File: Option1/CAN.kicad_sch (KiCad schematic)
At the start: 6 parts, among them U1 TJA1051T-3

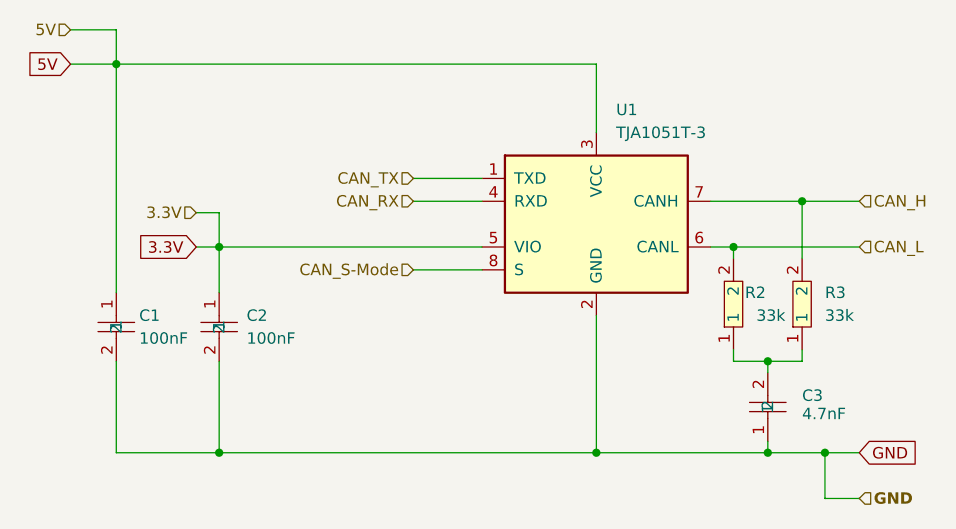
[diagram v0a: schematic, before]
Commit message: SPI Flash hinzugefügt, IN/Outputs vereinheitlicht, USB Flash Möglichkeit hinzugefügt, Display fehtl noch
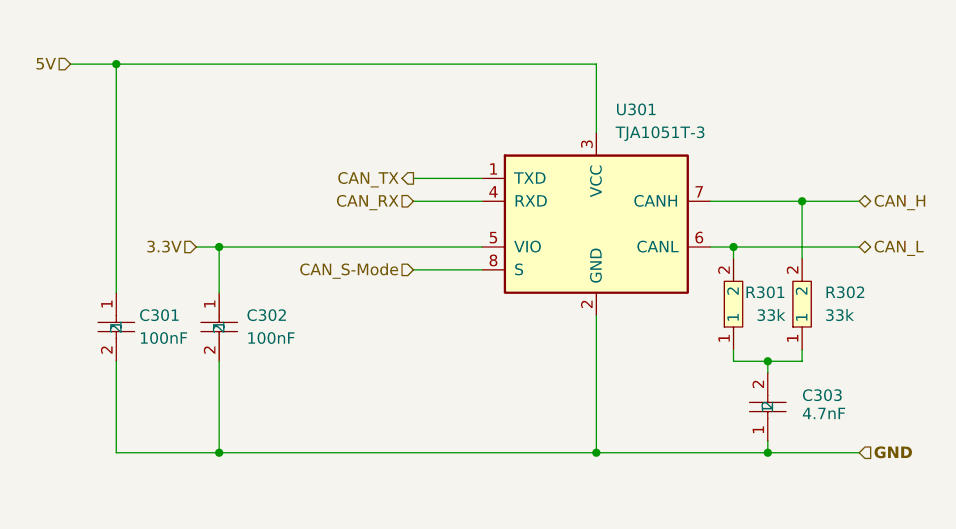
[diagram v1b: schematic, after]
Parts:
- renumbered C1 to C301, C2 to C302, C3 to C303, R2 to R301, R3 to R302, U1 to U301
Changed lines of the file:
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@@
 (kicad_sch
-	(version 20231120)
+	(version 20250114)
 	(generator "eeschema")
-	(generator_version "8.0")
+	(generator_version "9.0")
 	(paper "A4")
 	(title_block
@@
 	)
 	(junction
-		(at 167.64 121.92)
-		(diameter 0)
-		(color 0 0 0 0)
-	)
-	(junction
 		(at 161.29 111.76)
 		(diameter 0)
@@
 	(wire
 		(pts
-			(xy 167.64 121.92) (xy 161.29 121.92)
+			(xy 161.29 121.92) (xy 171.45 121.92)
 		)
 		(stroke
@@
 	(wire
 		(pts
-			(xy 171.45 121.92) (xy 167.64 121.92)
-		)
-		(stroke
-			(width 0)
-			(type default)
-		)
-	)
-	(wire
-		(pts
 			(xy 100.33 99.06) (xy 100.33 104.14)
 		)
@@
 	(wire
 		(pts
-			(xy 88.9 74.93) (xy 88.9 78.74)
-		)
-		(stroke
-			(width 0)
-			(type default)
-		)
-	)
-	(wire
-		(pts
 			(xy 157.48 99.06) (xy 171.45 99.06)
 		)
@@
 	(wire
 		(pts
-			(xy 97.79 95.25) (xy 100.33 95.25)
+			(xy 97.79 99.06) (xy 100.33 99.06)
 		)
 		(stroke
@@
 	(wire
 		(pts
-			(xy 167.64 127) (xy 167.64 121.92)
-		)
-		(stroke
-			(width 0)
-			(type default)
-		)
-	)
-	(wire
-		(pts
-			(xy 97.79 99.06) (xy 100.33 99.06)
-		)
-		(stroke
-			(width 0)
-			(type default)
-		)
-	)
-	(wire
-		(pts
 			(xy 165.1 111.76) (xy 161.29 111.76)
 		)
@@
 	(wire
 		(pts
-			(xy 83.82 74.93) (xy 88.9 74.93)
+			(xy 83.82 78.74) (xy 88.9 78.74)
 		)
 		(stroke
@@
 	(wire
 		(pts
-			(xy 171.45 127) (xy 167.64 127)
-		)
-		(stroke
-			(width 0)
-			(type default)
-		)
-	)
-	(wire
-		(pts
 			(xy 121.92 93.98) (xy 129.54 93.98)
 		)
@@
 	(wire
 		(pts
-			(xy 100.33 95.25) (xy 100.33 99.06)
-		)
-		(stroke
-			(width 0)
-			(type default)
-		)
-	)
-	(wire
-		(pts
 			(xy 154.94 99.06) (xy 157.48 99.06)
 		)
@@
 	(wire
 		(pts
-			(xy 88.9 78.74) (xy 83.82 78.74)
-		)
-		(stroke
-			(width 0)
-			(type default)
-		)
-	)
-	(wire
-		(pts
 			(xy 161.29 121.92) (xy 161.29 120.65)
 		)
@@
 			(width 0)
 			(type default)
-		)
-	)
-	(global_label "GND"
-		(shape input)
-		(at 171.45 121.92 0)
-		(fields_autoplaced yes)
-		(effects
-			(font
-				(size 1.27 1.27)
-			)
-			(justify left)
-		)
-		(property "Intersheetrefs" "${INTERSHEET_REFS}"
-			(at 178.3057 121.92 0)
-			(effects
-				(font
-					(size 1.27 1.27)
-				)
-				(justify left)
-				(hide yes)
-			)
-		)
-	)
-	(global_label "3.3V"
-		(shape input)
-		(at 97.79 99.06 180)
-		(fields_autoplaced yes)
-		(effects
-			(font
-				(size 1.27 1.27)
-			)
-			(justify right)
-		)
-		(property "Intersheetrefs" "${INTERSHEET_REFS}"
-			(at 90.6924 99.06 0)
-			(effects
-				(font
-					(size 1.27 1.27)
-				)
-				(justify right)
-				(hide yes)
-			)
-		)
-	)
-	(global_label "5V"
-		(shape input)
-		(at 83.82 78.74 180)
-		(fields_autoplaced yes)
-		(effects
-			(font
-				(size 1.27 1.27)
-			)
-			(justify right)
-		)
-		(property "Intersheetrefs" "${INTERSHEET_REFS}"
-			(at 78.5367 78.74 0)
-			(effects
-				(font
-					(size 1.27 1.27)
-				)
-				(justify right)
-				(hide yes)
-			)
 		)
 	)
@@
 	(hierarchical_label "GND"
 		(shape input)
-		(at 171.45 127 0)
+		(at 171.45 121.92 0)
 		(effects
 			(font
@@
 	)
 	(hierarchical_label "CAN_TX"
-		(shape input)
+		(shape output)
 		(at 121.92 91.44 180)
 		(effects
@@
 	(hierarchical_label "3.3V"
 		(shape input)
-		(at 97.79 95.25 180)
+		(at 97.79 99.06 180)
 		(effects
 			(font
@@
 	)
 	(hierarchical_label "CAN_L"
-		(shape input)
+		(shape bidirectional)
 		(at 171.45 99.06 0)
 		(effects
@@
 	(hierarchical_label "5V"
 		(shape input)
-		(at 83.82 74.93 180)
+		(at 83.82 78.74 180)
 		(effects
 			(font
@@
 	)
 	(hierarchical_label "CAN_H"
-		(shape input)
+		(shape bidirectional)
 		(at 171.45 93.98 0)
 		(effects
@@
 		(dnp no)
 		(fields_autoplaced yes)
-		(property "Reference" "U1"
-			(at 144.4341 83.82 0)
+		(property "Reference" "U301"
+			(at 144.3833 83.82 0)
 			(effects
 				(font
@@
 		)
 		(property "Value" "TJA1051T-3"
-			(at 144.4341 86.36 0)
+			(at 144.3833 86.36 0)
 			(effects
 				(font
@@
 			(project "Option1"
 				(path "/b9e5f262-9648-4b79-bdd1-af888b822329/09daa8db-a615-4efc-9912-47e942ec8e61"
-					(reference "U1")
+					(reference "U1701")
 					(unit 1)
 				)
@@
 		(on_board yes)
 		(dnp no)
-		(property "Reference" "R2"
+		(property "Reference" "R301"
 			(at 158.75 104.14 90)
 			(effects
@@
 			(project "Option1"
 				(path "/b9e5f262-9648-4b79-bdd1-af888b822329/09daa8db-a615-4efc-9912-47e942ec8e61"
-					(reference "R2")
+					(reference "R1701")
 					(unit 1)
 				)
 				(path "/b9e5f262-9648-4b79-bdd1-af888b822329/149ab29c-8f38-45ea-932f-f5c39c8a8ac3"
-					(reference "R?")
+					(reference "R301")
 					(unit 1)
 				)
@@
 		(on_board yes)
 		(dnp no)
-		(property "Reference" "C1"
+		(property "Reference" "C301"
 			(at 91.44 106.68 90)
 			(effects
@@
 			(project "Option1"
 				(path "/b9e5f262-9648-4b79-bdd1-af888b822329/09daa8db-a615-4efc-9912-47e942ec8e61"
-					(reference "C1")
+					(reference "C1701")
 					(unit 1)
 				)
 				(path "/b9e5f262-9648-4b79-bdd1-af888b822329/149ab29c-8f38-45ea-932f-f5c39c8a8ac3"
-					(reference "C?")
+					(reference "C301")
 					(unit 1)
 				)
@@
 		(on_board yes)
 		(dnp no)
-		(property "Reference" "C2"
+		(property "Reference" "C302"
 			(at 103.378 106.68 90)
 			(effects
@@
 			(project "Option1"
 				(path "/b9e5f262-9648-4b79-bdd1-af888b822329/09daa8db-a615-4efc-9912-47e942ec8e61"
-					(reference "C2")
+					(reference "C1702")
 					(unit 1)
 				)
@@
 		(on_board yes)
 		(dnp no)
-		(property "Reference" "C3"
+		(property "Reference" "C303"
 			(at 165.1 115.5699 90)
 			(effects
@@
 			(project "Option1"
 				(path "/b9e5f262-9648-4b79-bdd1-af888b822329/09daa8db-a615-4efc-9912-47e942ec8e61"
-					(reference "C3")
+					(reference "C1703")
 					(unit 1)
 				)
 				(path "/b9e5f262-9648-4b79-bdd1-af888b822329/149ab29c-8f38-45ea-932f-f5c39c8a8ac3"
-					(reference "C?")
+					(reference "C303")
 					(unit 1)
 				)
@@
 		(dnp no)
 		(fields_autoplaced yes)
-		(property "Reference" "R3"
+		(property "Reference" "R302"
 			(at 167.64 104.1399 90)
 			(effects
@@
 			(project "Option1"
 				(path "/b9e5f262-9648-4b79-bdd1-af888b822329/09daa8db-a615-4efc-9912-47e942ec8e61"
-					(reference "R3")
+					(reference "R1702")
 					(unit 1)
 				)
 				(path "/b9e5f262-9648-4b79-bdd1-af888b822329/149ab29c-8f38-45ea-932f-f5c39c8a8ac3"
-					(reference "R?")
-					(unit 1)
-				)
+					(reference "R302")
+					(unit 1)
+				)

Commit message: Erste issues eingearbeitet
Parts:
- added C304: 100nF, easyeda2kicad:C0603, symbol easyeda2kicad:CL10B104KA8NNNC
- added R204: 10kΩ, easyeda2kicad:R0603, symbol EasyEda2KiCad:0603WAF1002T5E
- added R303: 120Ω, easyeda2kicad:R0603, symbol EasyEda2KiCad:0603WAF1200T5E
- added U1: MCP2515-I/ST, easyeda2kicad:TSSOP-20_L6.5-W4.4-P0.65-LS6.4-BL, symbol EasyEda2KiCad:MCP2515-I_ST
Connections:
- net CAN_H: now also R303.2
- net CAN_L: now also R303.1
- net CAN_RX: now also U1.2 (RXCAN)
- net CAN_TX: now also U1.1 (TXCAN)
- net GND: now also C304.2, U1.10 (VSS)
- net 3.3V renamed 3V3
- net 3V3: now also C304.1, R204.2, U1.20 (VDD)
- new net: R204.1, U1.19 (~{RESET})
- new net SPI_CLK_CAN: U1.14 (SCK)
- new net SPI_CS_CAN: U1.18 (~{CS})
- new net SPI_INT_CAN: U1.13 (~{INT})
- new net SPI_MISO_CAN: U1.17 (SO)
- new net SPI_MOSI_CAN: U1.16 (SI)
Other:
- note added: "CAN to SPI"
- moved on the sheet: C301, C302, C303, R301, R302, U301

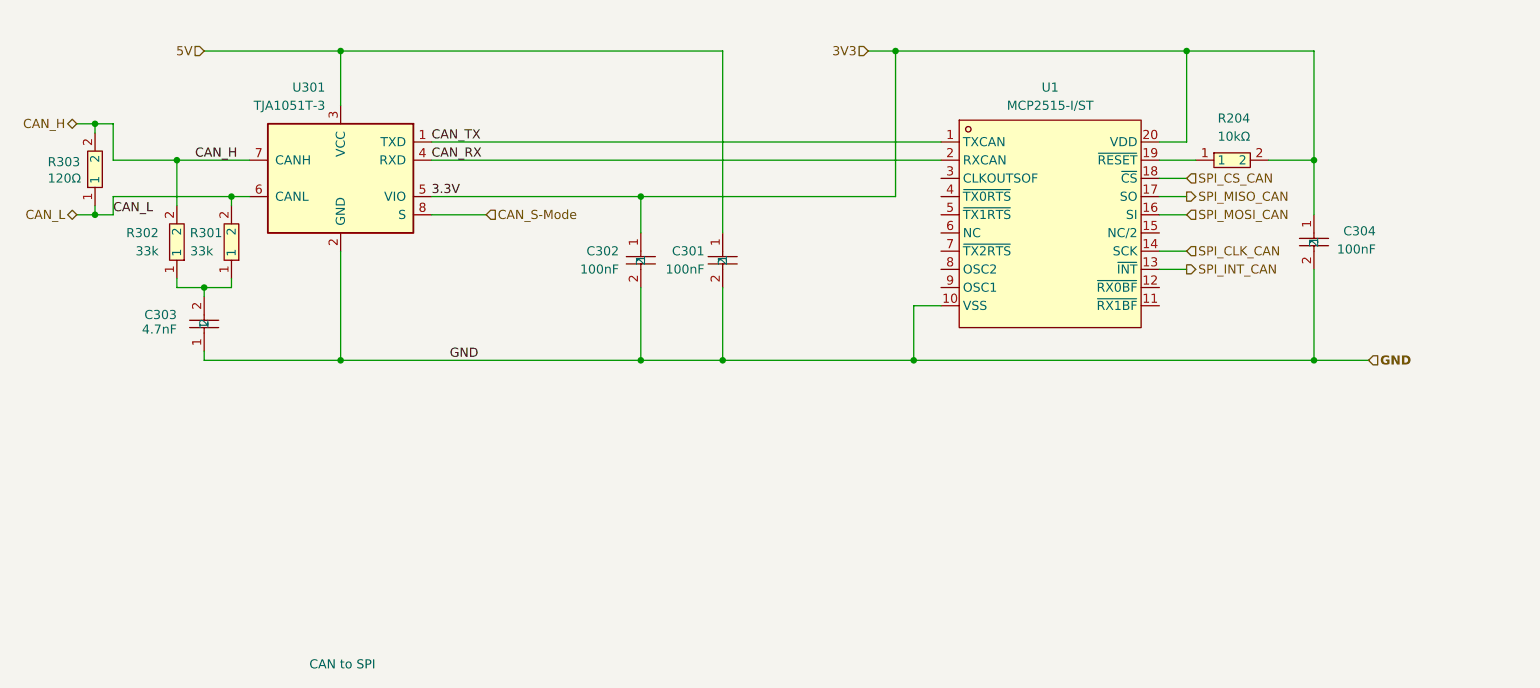
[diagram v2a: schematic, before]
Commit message: Oszillator für CAN-Controller hinzugefügt, Abschlusswiderstände eingefügt
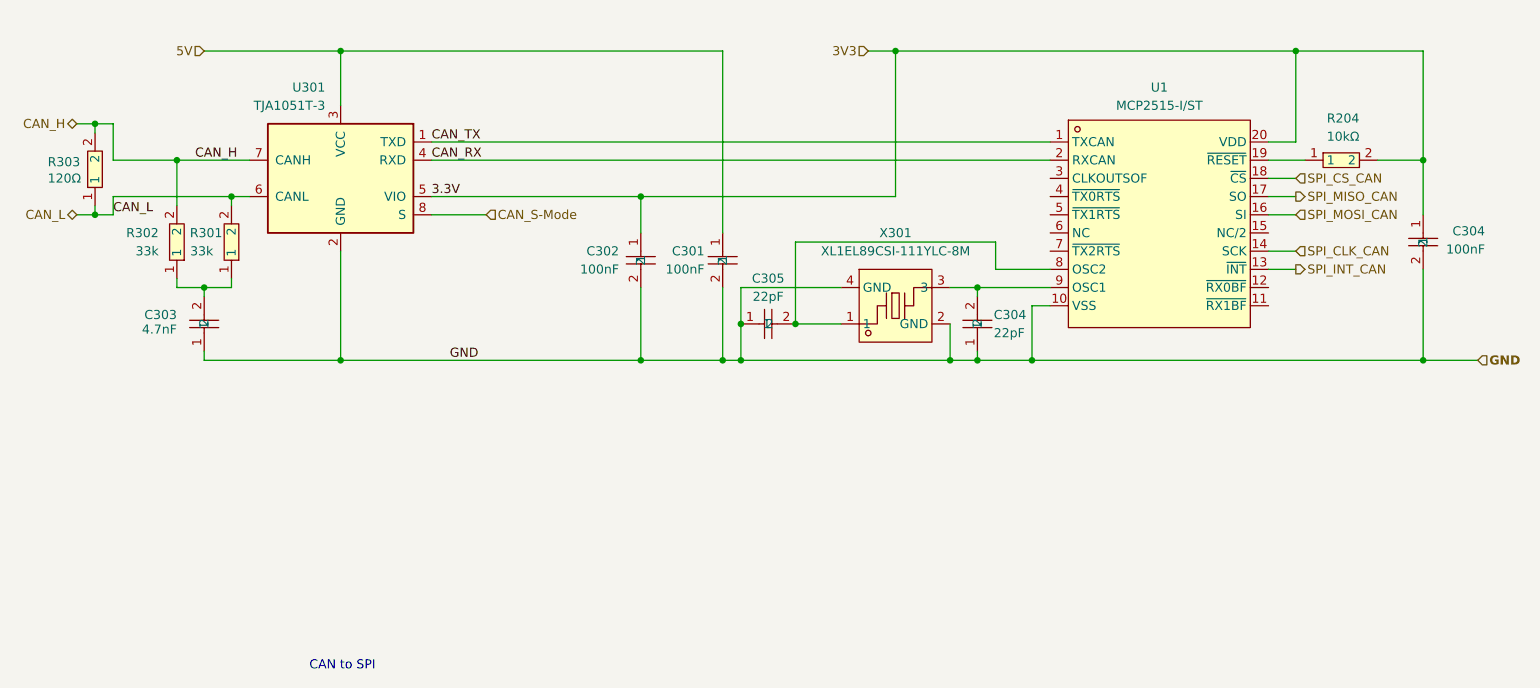
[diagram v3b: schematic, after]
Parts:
- added C304, C305: 22pF, easyeda2kicad:C0805, symbol EasyEda2KiCad:CL21C220JBANNNC
- added X301: XL1EL89CSI-111YLC-8M, easyeda2kicad:CRYSTAL-SMD_4P-L5.0-W3.2-BL-7I12288F20UCG, symbol EasyEda2KiCad:XL1EL89CSI-111YLC-8M
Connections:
- net GND: now also C304.1, C305.1, X301.2 (GND), X301.4 (GND)
- net at U1.8 (OSC2): now also C305.2, X301.1
- net at U1.9 (OSC1): now also C304.2, X301.3
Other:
- moved on the sheet: C304, R204, U1

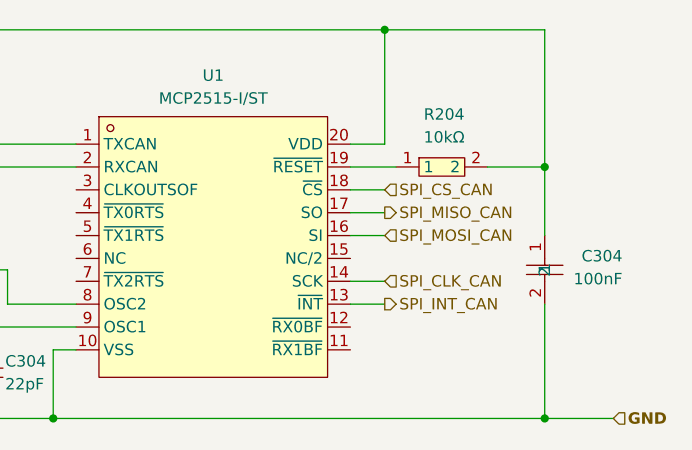
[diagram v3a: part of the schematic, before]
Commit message: USB Schaltung angepasst, Transistoren korrigiert, Stecker ausgetauscht, Dioden hinzugefügt
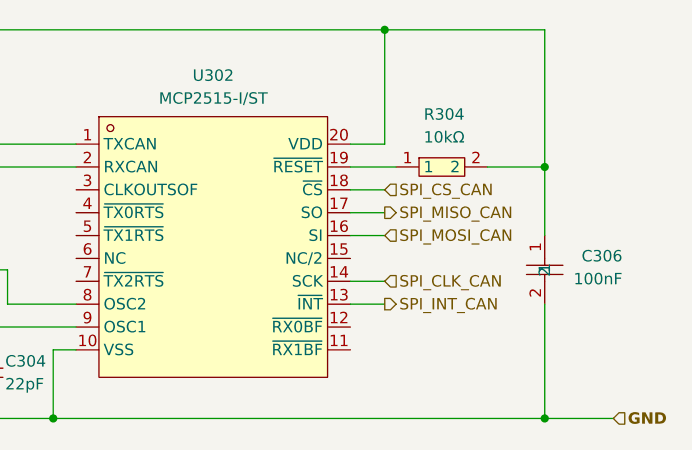
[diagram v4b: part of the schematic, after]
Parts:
- renumbered C304 to C306, R204 to R304, U1 to U302
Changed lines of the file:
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@@
 		(on_board yes)
 		(dnp no)
-		(property "Reference" "R204"
+		(property "Reference" "R304"
 			(at 254.254 88.138 0)
 			(effects
@@
 			(project ""
 				(path "/b9e5f262-9648-4b79-bdd1-af888b822329/149ab29c-8f38-45ea-932f-f5c39c8a8ac3"
-					(reference "R204")
+					(reference "R304")
 					(unit 1)
 				)
@@
 		(dnp no)
 		(fields_autoplaced yes)
-		(property "Reference" "U1"
+		(property "Reference" "U302"
 			(at 228.6 83.82 0)
 			(effects
@@
 			(project ""
 				(path "/b9e5f262-9648-4b79-bdd1-af888b822329/149ab29c-8f38-45ea-932f-f5c39c8a8ac3"
-					(reference "U1")
+					(reference "U302")
 					(unit 1)
 				)
@@
 		(on_board yes)
 		(dnp no)
-		(property "Reference" "C304"
+		(property "Reference" "C306"
 			(at 274.066 103.886 90)
 			(effects
@@
 			(project "Option1"
 				(path "/b9e5f262-9648-4b79-bdd1-af888b822329/149ab29c-8f38-45ea-932f-f5c39c8a8ac3"
-					(reference "C304")
-					(unit 1)
-				)
+					(reference "C306")
+					(unit 1)
+				)

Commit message: GND polygon hinzugefügt, unverbundene Pads verknüpft, 0 Ohm Widerstand für Display Strohmversorgung hinzugefügt
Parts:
- removed C303: 4.7nF, easyeda2kicad:C0805, symbol easyeda2kicad:0805B472K500NT
- removed R301, R302: 33k, easyeda2kicad:R0603, symbol easyeda2kicad:0603WAF3302T5E
